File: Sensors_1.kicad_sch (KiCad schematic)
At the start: 13 parts, among them U3 Ai-Thinker-Ra-01

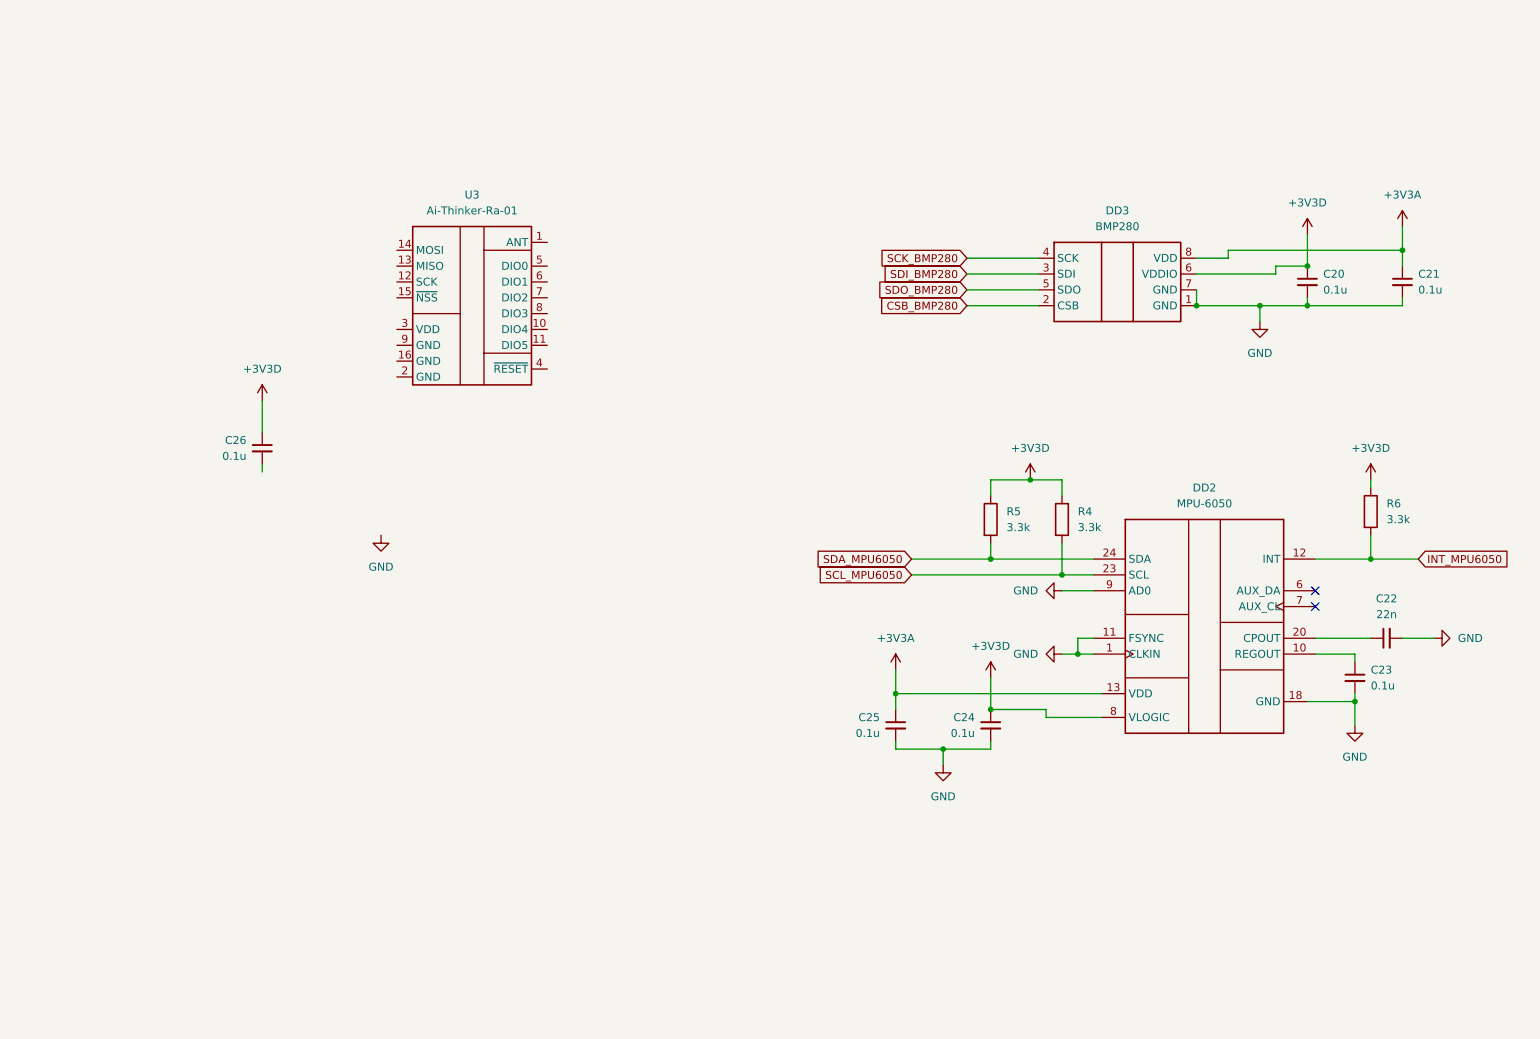
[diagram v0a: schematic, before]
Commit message: feat: added connection for sensors
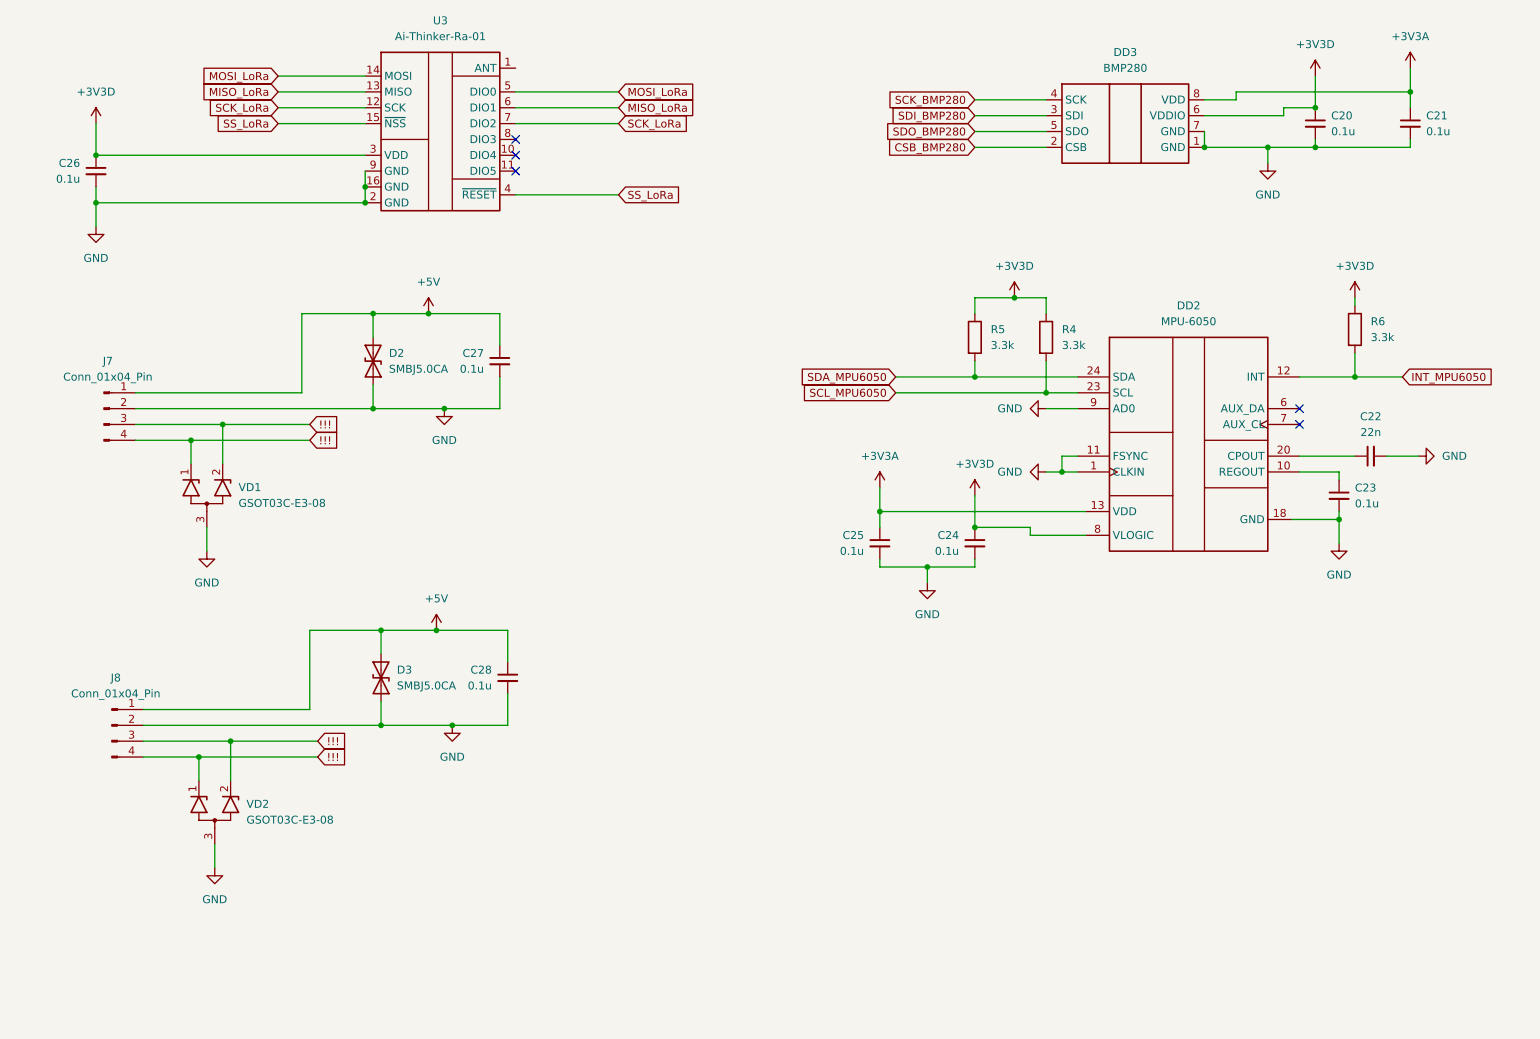
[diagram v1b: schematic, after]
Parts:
- added C27, C28: 0.1u, Capacitor_SMD:C_0805_2012Metric_Pad1.18x1.45mm_HandSolder, symbol Device:C_Small
- added D2, D3: SMBJ5.0CA, Diode_SMD:D_SMB_Handsoldering, symbol TVS:SMBJ5.0CA
- added J7, J8: Conn_01x04_Pin, Connector_PinHeader_2.54mm:PinHeader_1x04_P2.54mm_Horizontal, symbol Connector:Conn_01x04_Pin
- added VD1, VD2: GSOT03C-E3-08, Package_TO_SOT_SMD:SOT-23_Handsoldering, symbol TWS:GSOT03C-E3-08
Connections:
- net +3V3D: now also U3.3 (VDD)
- net GND: now also C26.2, U3.16 (GND), U3.2 (GND), U3.9 (GND), C27.2, C28.2, D2.1 (A1), D3.1 (A1), J7.2 (Pin_2), J8.2 (Pin_2), VD1.3 (A), VD2.3 (A)
- net SCK_LoRa: now reaches U3.12 (SCK)
- net SCK_LoRa: now also U3.7 (DIO2)
- net MISO_LoRa: now reaches U3.13 (MISO)
- net MISO_LoRa: now also U3.6 (DIO1)
- net MOSI_LoRa: now reaches U3.14 (MOSI)
- net MOSI_LoRa: now also U3.5 (DIO0)
- net SS_LoRa: now reaches U3.15 (~{NSS})
- net SS_LoRa: now also U3.4 (~{RESET})
- new net !!!: J7.3 (Pin_3), J7.4 (Pin_4), J8.3 (Pin_3), J8.4 (Pin_4), VD1.1 (K1), VD1.2 (K2), VD2.1 (K1), VD2.2 (K2)
- new net +5V: C27.1, C28.1, D2.2 (A2), D3.2 (A2), J7.1 (Pin_1), J8.1 (Pin_1)
- no-connect marks 2 -> 5
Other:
- moved on the sheet: C20, C21, C22, C23, C24, C25, C26, DD2, DD3, R4, R5, R6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

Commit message: feat: firs complete version schemattic
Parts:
- removed J8: Conn_01x04_Pin, Connector_PinHeader_2.54mm:PinHeader_1x04_P2.54mm_Horizontal, symbol Connector:Conn_01x04_Pin
- added J8: Conn_01x06_Pin, Connector_Hirose:Hirose_DF13-06P-1.25DSA_1x06_P1.25mm_Vertical, symbol Connector:Conn_01x06_Pin
- added J9: Conn_01x02_Pin, Connector_Hirose:Hirose_DF13-02P-1.25DSA_1x02_P1.25mm_Vertical, symbol Connector:Conn_01x02_Pin
- added R7, R8: 3.3k, Resistor_SMD:R_0805_2012Metric_Pad1.20x1.40mm_HandSolder, symbol Device:R
- added VD3: GSOT03C-E3-08, Package_TO_SOT_SMD:SOT-23_Handsoldering, symbol TWS:GSOT03C-E3-08
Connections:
- net +3V3D: now also R7.1, R8.1
- net +5V: now also J8.1 (Pin_1)
- net GND: now also J8.6 (Pin_6), VD3.3 (A)
- removed net !!!: J7.3 (Pin_3), J7.4 (Pin_4), VD1.1 (K1), VD1.2 (K2), VD2.1 (K1), VD2.2 (K2)
- new net BN_880_RX: J8.3 (Pin_3), VD2.1 (K1)
- new net BN_880_SCL: J9.2 (Pin_2), R7.2, VD3.1 (K1)
- new net BN_880_SDA: J9.1 (Pin_1), R8.2, VD3.2 (K2)
- new net BN_880_TX: J8.2 (Pin_2), VD2.2 (K2)
- new net HC_echo: J7.4 (Pin_4), VD1.1 (K1)
- new net HC_trigger: J7.3 (Pin_3), VD1.2 (K2)
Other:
- moved on the sheet: C28, D3, VD2

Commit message: feat: Added part of the connections (digital data lines) of the microcontroller
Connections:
- net MISO_LoRa: no longer U3.6 (DIO1)
- net MOSI_LoRa: no longer U3.5 (DIO0)
- net SCK_LoRa: no longer U3.7 (DIO2)
- net SS_LoRa: no longer U3.4 (~{RESET})
- new net DIO0_LoRa: U3.5 (DIO0)
- new net DIO1_LoRa: U3.6 (DIO1)
- new net DIO2_LoRa: U3.7 (DIO2)
- new net Reset_LoRa: U3.4 (~{RESET})
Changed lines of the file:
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@@
+	)
+	(junction
+		(at 101.6 123.19)
+		(diameter 0)
+		(color 0 0 0 0)
 	)
 	(junction
@@
 	(junction
 		(at 68.58 156.21)
-		(diameter 0)
-		(color 0 0 0 0)
-	)
-	(junction
-		(at 101.6 123.19)
 		(diameter 0)
 		(color 0 0 0 0)
@@
 	(wire
 		(pts
-			(xy 101.6 123.19) (xy 121.92 123.19)
+			(xy 101.6 123.19) (xy 115.57 123.19)
 		)
 		(stroke
@@
 		)
 	)
-	(global_label "MISO_LoRa"
+	(global_label "DIO1_LoRa"
 		(shape input)
 		(at 121.92 36.83 0)
@@
 		)
 		(property "Intersheetrefs" "${INTERSHEET_REFS}"
-			(at 135.0651 36.83 0)
+			(at 134.8837 36.83 0)
 			(hide yes)
 			(show_name no)
@@
 	(global_label "BN_880_TX"
 		(shape input)
-		(at 121.92 123.19 0)
+		(at 115.57 123.19 0)
 		(fields_autoplaced yes)
 		(effects
@@
 		)
 		(property "Intersheetrefs" "${INTERSHEET_REFS}"
-			(at 135.2465 123.19 0)
+			(at 128.8965 123.19 0)
 			(hide yes)
 			(show_name no)
@@
 		)
 	)
-	(global_label "MOSI_LoRa"
+	(global_label "DIO0_LoRa"
 		(shape input)
 		(at 121.92 34.29 0)
@@
 		)
 		(property "Intersheetrefs" "${INTERSHEET_REFS}"
-			(at 135.0651 34.29 0)
+			(at 134.8837 34.29 0)
 			(hide yes)
 			(show_name no)
@@
 		)
 	)
-	(global_label "SCK_LoRa"
+	(global_label "DIO2_LoRa"
 		(shape input)
 		(at 121.92 39.37 0)
@@
 		)
 		(property "Intersheetrefs" "${INTERSHEET_REFS}"
-			(at 134.2184 39.37 0)
+			(at 134.8837 39.37 0)
 			(hide yes)
 			(show_name no)
@@
 		)
 	)
-	(global_label "SS_LoRa"
+	(global_label "Reset_LoRa"
 		(shape input)
 		(at 121.92 50.8 0)
@@
 		)
 		(property "Intersheetrefs" "${INTERSHEET_REFS}"
-			(at 132.8879 50.8 0)
+			(at 135.6699 50.8 0)
 			(hide yes)
 			(show_name no)

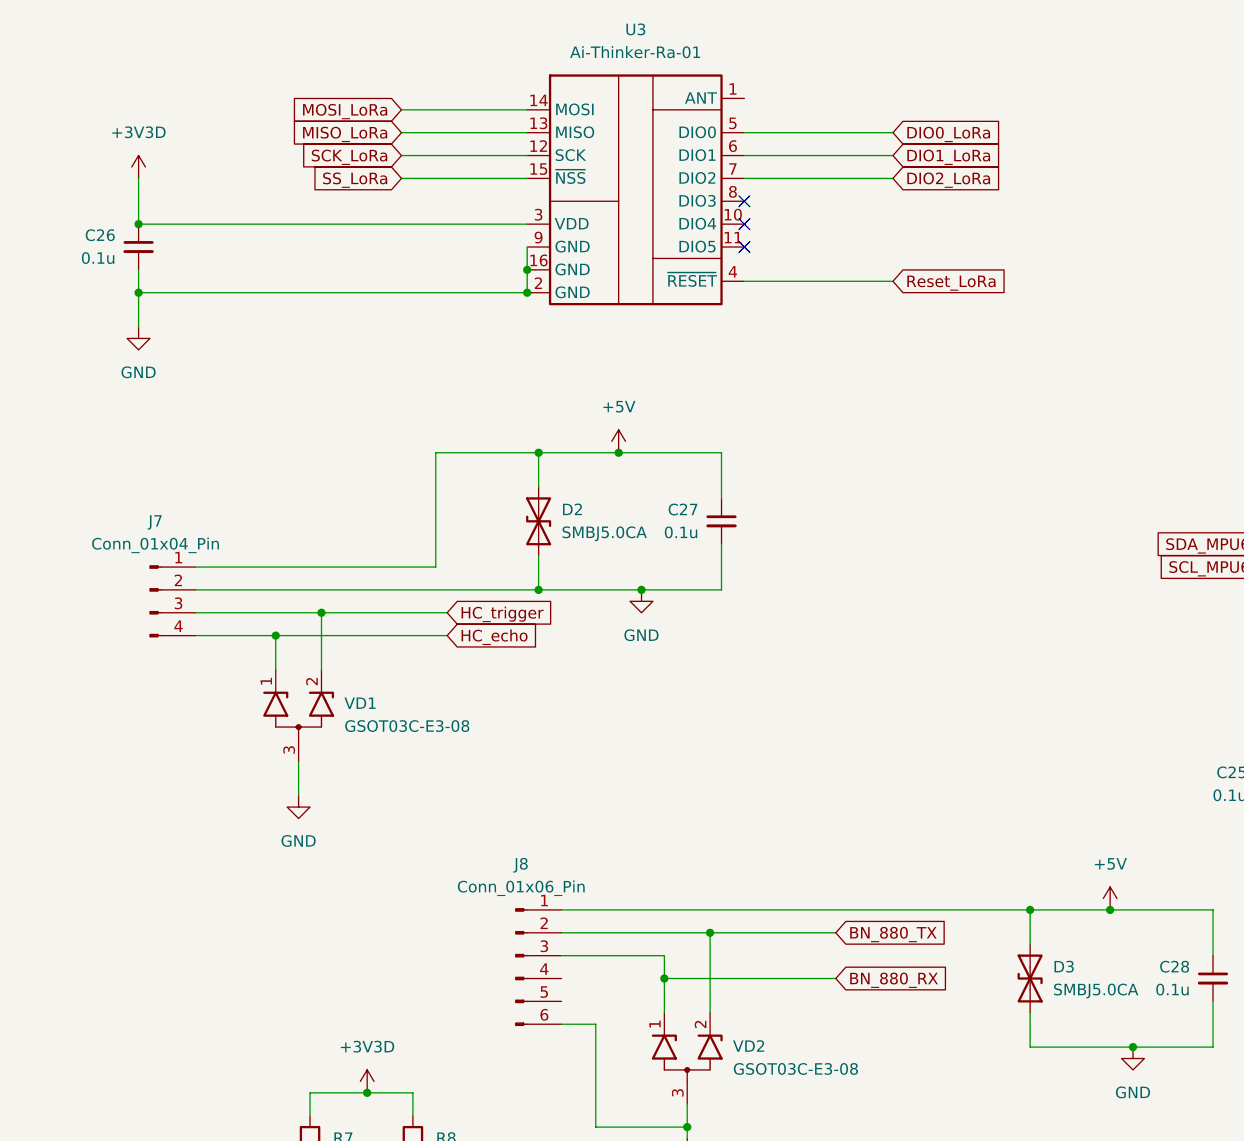
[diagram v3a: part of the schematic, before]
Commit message: feat: complete schematic, and start PCB
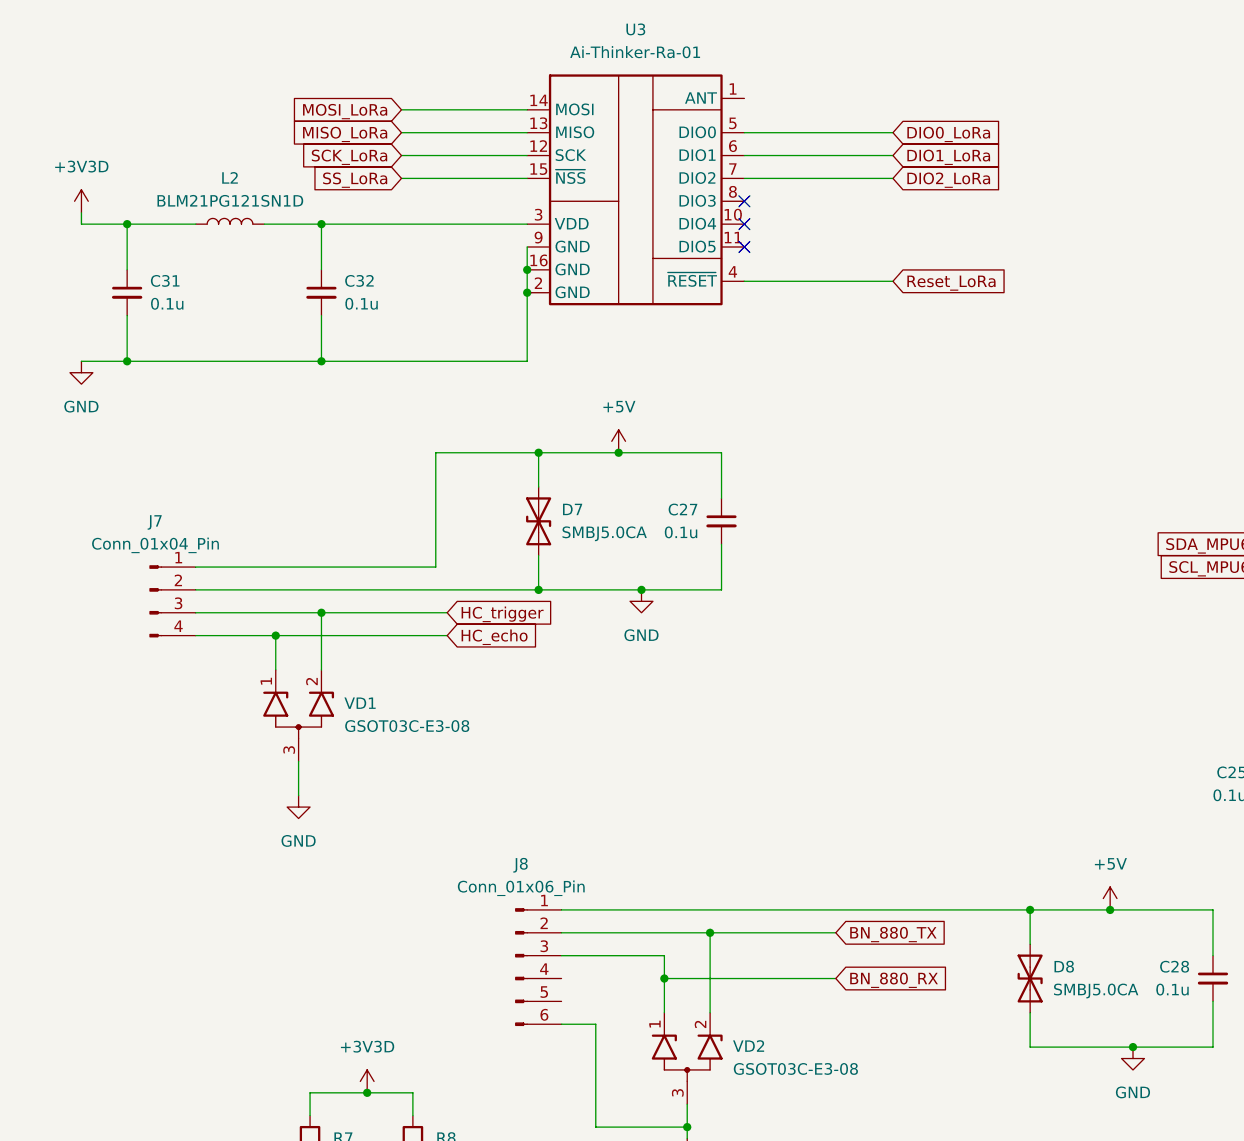
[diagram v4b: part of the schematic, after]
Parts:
- removed C26: 0.1u, Capacitor_SMD:C_0805_2012Metric_Pad1.18x1.45mm_HandSolder, symbol Device:C_Small
- removed D2, D3: SMBJ5.0CA, Diode_SMD:D_SMB_Handsoldering, symbol TVS:SMBJ5.0CA
- added C31, C32: 0.1u, Capacitor_SMD:C_0805_2012Metric_Pad1.18x1.45mm_HandSolder, symbol Device:C_Small
- added D7, D8: SMBJ5.0CA, Diode_SMD:D_SMB_Handsoldering, symbol TVS:SMBJ5.0CA
- added L2: BLM21PG121SN1D, Inductor_SMD:L_0805_2012Metric_Pad1.05x1.20mm_HandSolder, symbol Inductors:L
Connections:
- net +3V3D: now also C31.1, L2.1; no longer U3.3 (VDD)
- net +5V: now also D7.2 (A2), D8.2 (A2)
- net GND: now also C31.2, C32.2, D7.1 (A1), D8.1 (A1)
- new net: C32.1, L2.2, U3.3 (VDD)

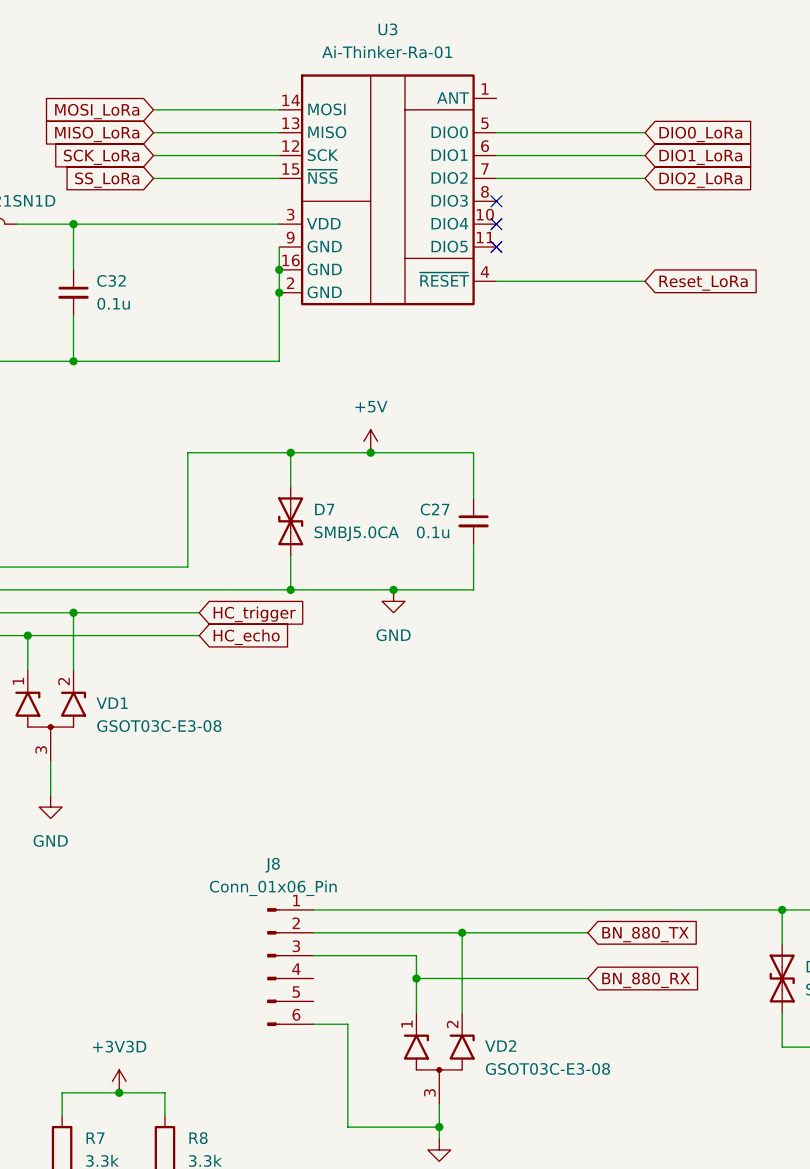
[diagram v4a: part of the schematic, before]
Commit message: feat: added mani lines for GND
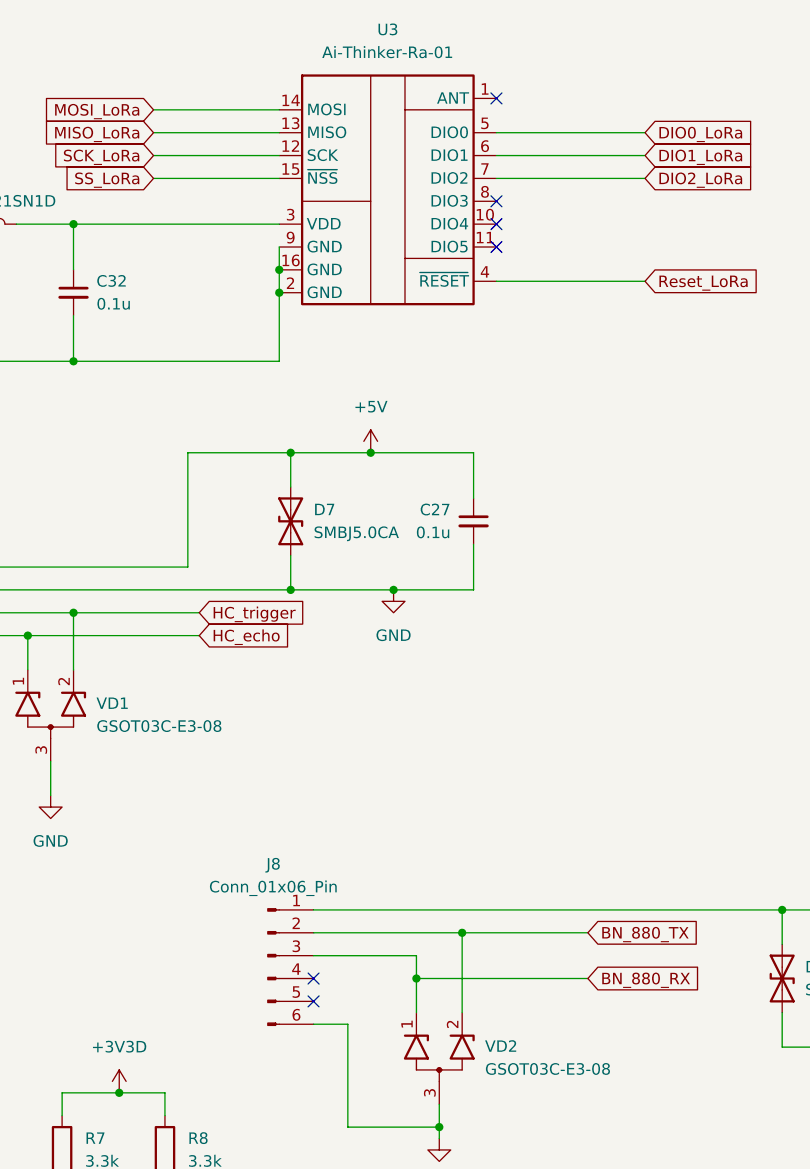
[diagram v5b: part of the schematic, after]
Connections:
- no-connect marks 5 -> 8
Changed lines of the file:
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@@
+	)
+	(no_connect
+		(at 85.09 128.27)
 	)
 	(no_connect
@@
 	)
 	(no_connect
+		(at 85.09 130.81)
+	)
+	(no_connect
+		(at 105.41 30.48)
+	)
+	(no_connect
